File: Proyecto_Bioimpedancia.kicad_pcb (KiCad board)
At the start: 2 copper layers, 100 x 100 mm, 69 parts, among them J1 Jumper, J2 Jumper, J3 Jumper_Calibration, J4 Jumper, J5 Jumper, J6 Jumper, P1 SD_LAPIZ, P10 RS-232, P11 SOURCE_2, P12 RESET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

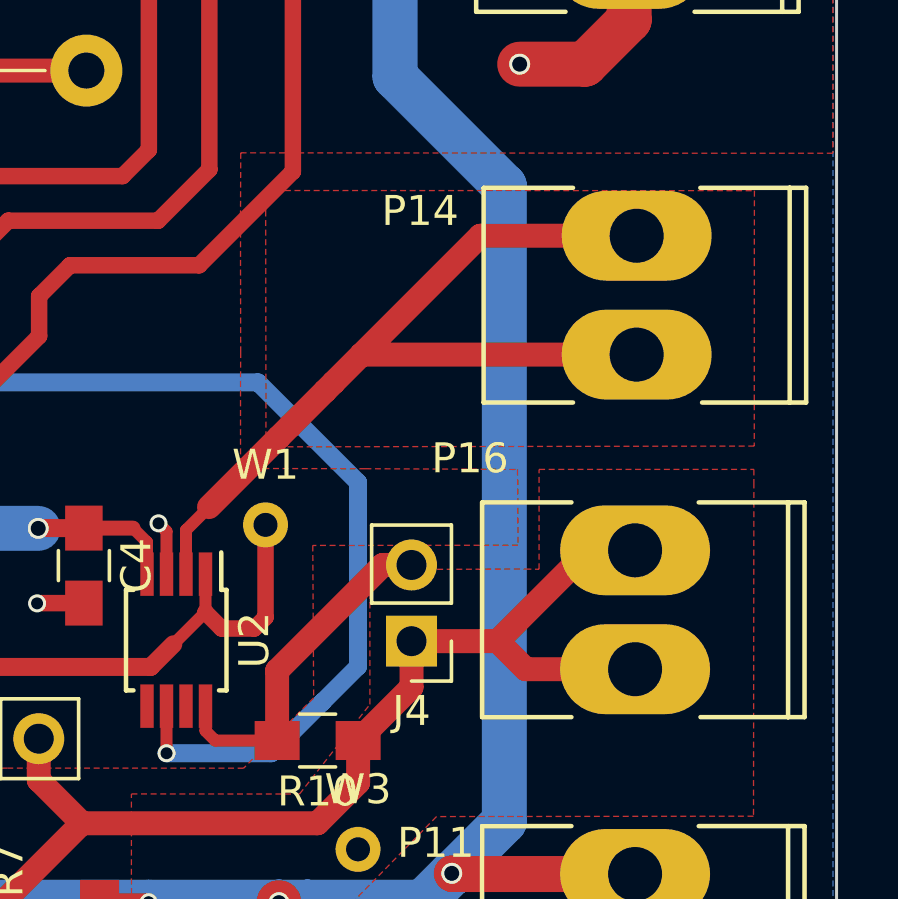
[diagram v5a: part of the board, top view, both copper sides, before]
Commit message: Conectores SMA actualizados
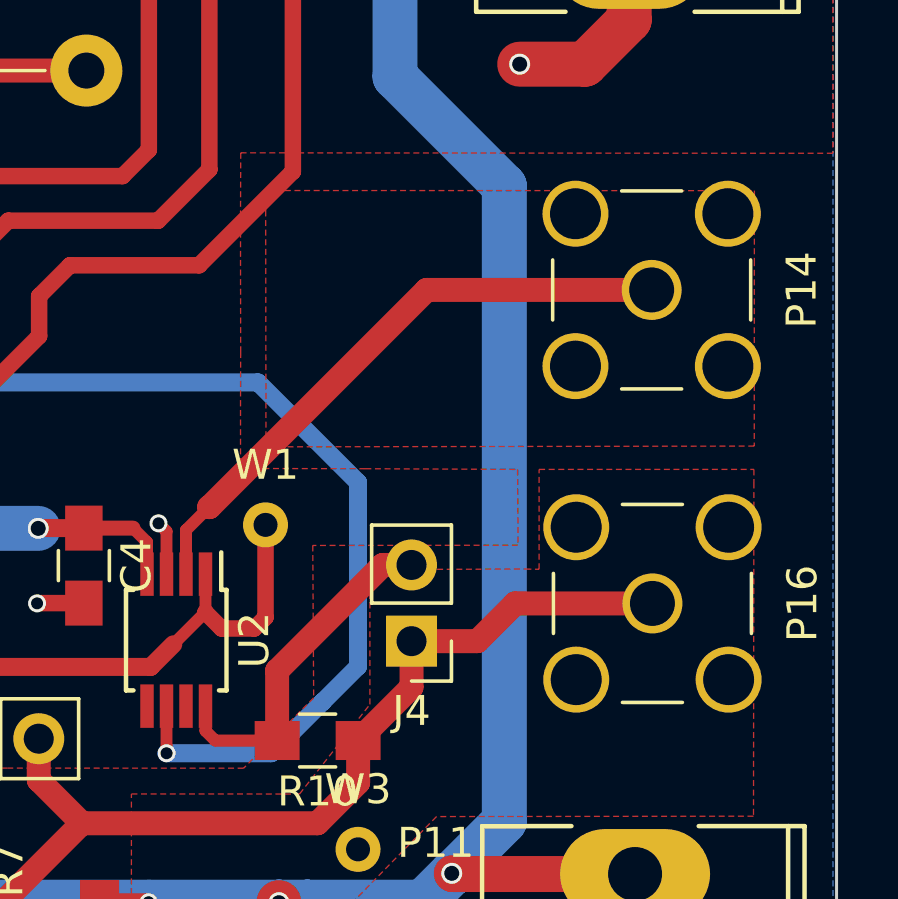
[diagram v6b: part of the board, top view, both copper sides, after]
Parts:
- P14, P16: footprint Sockets_MOLEX_KK-System:Socket_MOLEX-KK-RM3-96mm_Lock_2pin_straight -> Connectors:SMA_THT_Jack_Straight
- moved P16 0.62 mm to (180.4, 83.7)
- moved P14 0.53 mm to (180.4, 73.2)
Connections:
- P14 pad 2: /Z_UK -> (no net)
- P16 pad 2: /SIGNAL_A2 -> (no net)
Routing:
- net /Z_UK: track 29.7 -> 20.3 mm
- net /SIGNAL_A2: track 43.8 -> 38.7 mm

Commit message: PCB BIO mejorada con puertos I2C y capacitor para el puerto DTR del programador FTDI
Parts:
- removed P7: I2C_2, Socket_Strips:Socket_Strip_Straight_1x02_Pitch2.54mm
- added C14: 0,1uF, Capacitors_SMD:C_0805_HandSoldering, F.Cu at (165.7, 53.0)
- P10: footprint Socket_Strips:Socket_Strip_Straight_1x03_Pitch2.54mm -> Socket_Strips:Socket_Strip_Straight_1x04_Pitch2.54mm
- P6: value I2C_1 -> CONN_02X04; footprint Socket_Strips:Socket_Strip_Straight_1x02_Pitch2.54mm -> Socket_Strips:Socket_Strip_Straight_2x04_Pitch2.54mm
- moved P6 7.49 mm to (94.8, 82.2)
- moved P12 2.09 mm to (169.7, 48.8)
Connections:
- P6 pad 1: /SDA_R -> /SCL_R
- P6 pad 2: /SCL_R -> /SDA_R
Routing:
- net /SCL_R: track 56.0 -> 42.8 mm, vias 3 -> 2
- net /SDA_R: track 47.7 -> 37.6 mm
- net /RESET: track 89.0 -> 92.3 mm
- net Net-(C14-Pad1): track 0.00 -> 2.94 mm

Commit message: Revert "PCB BIO mejorada con puertos I2C y capacitor para el puerto DTR del programador FTDI"
This reverts commit 0fb084b6cb4dcbd826a5771fbeb8258d6327cef0.
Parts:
- removed C14: 0,1uF, Capacitors_SMD:C_0805_HandSoldering
- added P7: I2C_2, Socket_Strips:Socket_Strip_Straight_1x02_Pitch2.54mm, F.Cu at (92.3, 82.0)
- P10: footprint Socket_Strips:Socket_Strip_Straight_1x04_Pitch2.54mm -> Socket_Strips:Socket_Strip_Straight_1x03_Pitch2.54mm
- P6: value CONN_02X04 -> I2C_1; footprint Socket_Strips:Socket_Strip_Straight_2x04_Pitch2.54mm -> Socket_Strips:Socket_Strip_Straight_1x02_Pitch2.54mm
- moved P6 7.49 mm to (92.3, 89.3)
- moved P12 2.09 mm to (167.6, 48.8)
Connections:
- P6 pad 1: /SCL_R -> /SDA_R
- P6 pad 2: /SDA_R -> /SCL_R
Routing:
- net /SCL_R: track 42.8 -> 56.0 mm, vias 2 -> 3
- net /SDA_R: track 37.6 -> 47.7 mm
- net /RESET: track 92.3 -> 89.0 mm
- net Net-(C14-Pad1): track 2.94 -> 0.00 mm
